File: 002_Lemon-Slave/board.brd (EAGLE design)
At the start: 85.1 x 67 mm, 61 parts, among them IC1 74HC595N, IC2 74HC595N, IC3 74HC595N, IC4 7805TV, U1 ATTINY85-20P, X1 MKDSN1,5/2-5,08, X2 MKDSN1,5/2-5,08, X3 MKDSN1,5/2-5,08

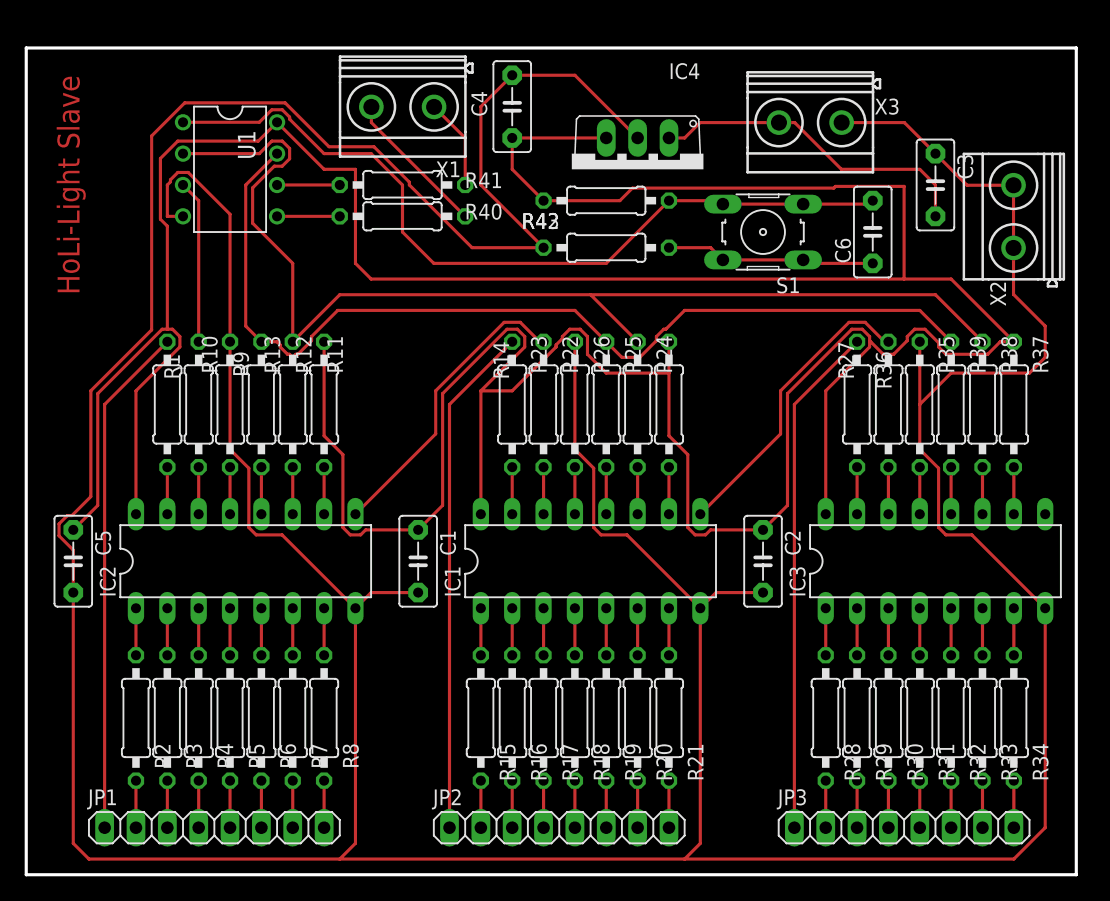
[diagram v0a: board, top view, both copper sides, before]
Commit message: fixed error in lemon-light slave controller
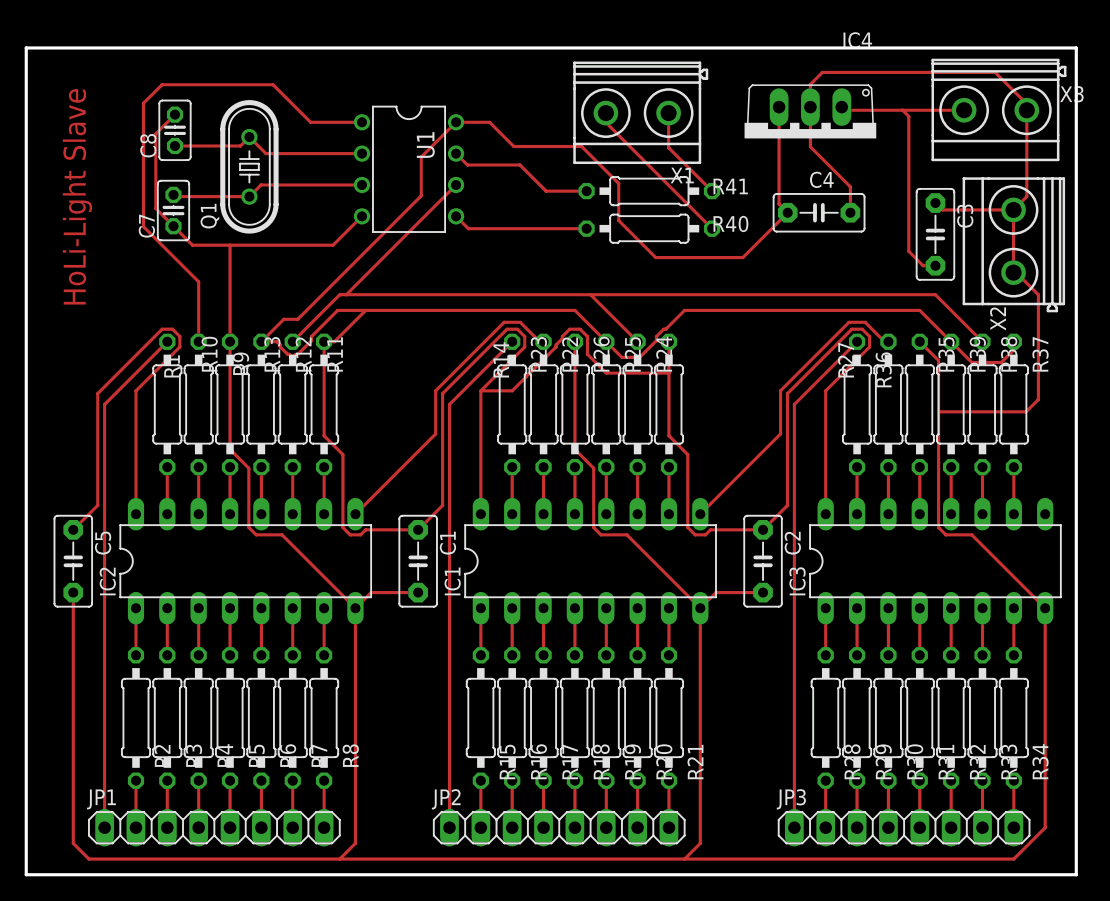
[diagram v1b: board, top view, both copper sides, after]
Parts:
- removed C6: 100n, capacitor-wima:C5B3
- removed R42: 1K, resistor:0207/10
- removed R43: 10K, resistor:0207/10
- removed S1: (no value), switch-omron:B3F-10XX
- added C7, C8: 22pF, resistor:C025-025X050
- added Q1: 14,7456, crystal:HC49/S
- moved C4 26.3 mm to (64.2, 53.6), turned to 180 degrees
- moved R40 20.0 mm to (50.5, 52.3)
- moved R41 20.0 mm to (50.5, 55.4)
- moved X1 19.0 mm to (49.5, 61.7)
- moved X3 15.0 mm to (78.5, 62.0)
- moved U1 14.5 mm to (31.0, 57.1)
- moved IC4 14.2 mm to (63.5, 59.6)
- moved C3 4.00 mm to (73.7, 51.9)
- moved X2 2.00 mm to (80.0, 51.3)
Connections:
- removed net N$68: R13.1, R26.1, R39.1, U1.7
- removed net N$75: C6.2, R42.2, S1.3, S1.4, U1.1
- new net N$78: C8.1, Q1.2, U1.2
- net +5V: now also R13.1, R26.1, R39.1; no longer R42.1
- net GND: now also C7.1, C8.2; no longer R43.1
- net N$67: now also U1.6; no longer U1.2
- net N$70: now also U1.7; no longer U1.6
- net N$73: now also U1.1; no longer U1.3
- net N$74: now also C7.2, Q1.1, U1.3; no longer C6.1, R43.2, S1.1, S1.2
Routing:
- net N$68: track 79.5 -> 0.00 mm
- net N$75: track 66.1 -> 0.00 mm
- net GND: track 424.4 -> 358.5 mm
- net N$73: track 13.2 -> 40.8 mm
- net +5V: track 336.4 -> 318.3 mm
- net N$78: track 0.00 -> 16.0 mm
- net N$67: track 92.4 -> 77.0 mm
- net N$70: track 5.08 -> 11.8 mm
- net N$69: track 5.08 -> 11.0 mm
- net N$72: track 26.7 -> 24.3 mm
- net N$74: track 17.0 -> 15.7 mm
- net N$66: track 12.0 -> 12.9 mm

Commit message: update lemon light main controller
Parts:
- removed U1: ATTINY85-20P, attiny25_45_85:PDIP08_300MIL
- added C6: 4,7nF, rcl:C0805K
- added JP4: (no value), pinhead:1X03
- added R42: 1K, resistor:M0805
- added R43: 10K, resistor:M0805
- added S1: (no value), switch-omron:B3F-10XX
- added U$1: ATTINY406, My_AVRs:SO20L
- C1, C2, C3, C4, C5: device capacitor-wima:C5B3 -> rcl:C0805K
- C7, C8: value 22pF -> 12pF; device resistor:C025-025X050 -> rcl:C0805K
- IC1, IC2, IC3: value 74HC595N -> 74HC595D; device 74xx-eu:DIL16 -> 74xx-eu:SO16
- Q1: device crystal:HC49/S -> crystal:SM49
- R1, R10, R11, R12, R13, R14, R15, R16, R17, R18, R19, R2, R20, R21, R22, R23, R24, R25, R26, R27, R28, R29, R3, R30, R31, R32, R33, R34, R35, R36, R37, R38, R39, R4, R5, R6, R7, R8, R9: device resistor:0207/10 -> resistor:M0805
- R40, R41: value 500 -> 100; device resistor:0207/10 -> resistor:M0805
- X1, X2, X3: value MKDSN1,5/2-5,08 -> (none)
- moved C3 28.1 mm to (47.1, 42.7), turned to 0 degrees
- moved C8 27.9 mm to (9.81, 32.5), turned to 0 degrees
- moved R40 24.8 mm to (28.5, 40.8)
- moved Q1 24.3 mm to (3.92, 37.6), turned to 270 degrees
- moved C4 24.2 mm to (42.7, 42.6)
- moved IC4 23.8 mm to (45.0, 44.6)
- moved X3 23.8 mm to (60.0, 47.0)
- moved X1 23.8 mm to (31.0, 46.7)
- moved R41 22.3 mm to (33.5, 40.9)
- moved X2 17.2 mm to (70.0, 37.3)
- moved R39 17.0 mm to (63.4, 25.6)
- moved R27 17.0 mm to (55.8, 25.6)
- moved R35 17.0 mm to (60.9, 25.6)
- moved R37 17.0 mm to (68.5, 25.6)
- moved R38 17.0 mm to (66.0, 25.6)
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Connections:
- new net N$68: R13.1, R26.1, R39.1, U$1.12
- new net N$75: C6.1, JP4.2, R43.2, S1.1, S1.2, U$1.16
- new net N$76: C6.2, R42.2, S1.3, S1.4
- net +5V: now also JP4.1, R43.1, U$1.1; no longer R13.1, R26.1, R39.1, U1.8
- net GND: now also JP4.3, R42.1, U$1.20; no longer U1.4
- net N$67: now also U$1.13; no longer U1.6
- net N$69: now also U$1.8; no longer U1.5
- net N$70: now also U$1.9; no longer U1.7
- net N$73: now also U$1.14; no longer U1.1
- net N$74: now also U$1.19; no longer U1.3
- net N$78: now also U$1.6; no longer U1.2
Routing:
- net +5V: track 318.3 -> 216.0 mm, vias 0 -> 8
- net GND: track 358.5 -> 276.6 mm, vias 0 -> 9
- net N$68: track 0.00 -> 66.4 mm
- net N$75: track 0.00 -> 42.9 mm
- net N$73: track 40.8 -> 19.1 mm, vias 0 -> 2
- net N$74: track 15.7 -> 33.5 mm
- net N$70: track 11.8 -> 29.0 mm, vias 0 -> 2
- net N$56: track 41.5 -> 26.6 mm
- net N$35: track 41.5 -> 26.9 mm
- net N$76: track 0.00 -> 14.2 mm
- net N$14: track 41.5 -> 27.8 mm
- net N$69: track 11.0 -> 23.7 mm, vias 0 -> 2
- net N$72: track 24.3 -> 14.8 mm
- net N$66: track 12.9 -> 6.27 mm
- net N$67: track 77.0 -> 71.1 mm, vias 0 -> 4
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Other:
- board size 85.1 x 67 mm -> 75.1 x 52.5 mm
- board text added: "GND"
- board text added: "HoLi-Light Slave from Michael Hohenstein"
- board text added: "Rx"
- board text added: "Tx"
- board text added: "VCC"
- board text removed: "HoLi-Light Slave"
